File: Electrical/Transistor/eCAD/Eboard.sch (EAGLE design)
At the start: 22 parts

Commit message: put resistor in series and resolved trace issues on board
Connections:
- new net N$1: D1.C, R4.1
- net 5V: no longer R4.2
- net GND: now also R4.2; no longer D1.C, R4.1
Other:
- moved on the sheet: D1, R4
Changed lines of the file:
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@@
 <instance part="JP6" gate="A" x="116.84" y="170.18" rot="R180"/>
 <instance part="STEER_ENC" gate="A" x="203.2" y="76.2"/>
-<instance part="D1" gate="G$1" x="83.82" y="86.36" rot="R90"/>
+<instance part="D1" gate="G$1" x="86.36" y="96.52"/>
 <instance part="LIGHT_A_B" gate="G$1" x="193.04" y="121.92"/>
-<instance part="R4" gate="G$1" x="86.36" y="96.52" rot="R180"/>
+<instance part="R4" gate="G$1" x="86.36" y="86.36" rot="R270"/>
 <instance part="GND1" gate="1" x="134.62" y="55.88"/>
 <instance part="GND3" gate="1" x="147.32" y="116.84"/>
-<instance part="GND4" gate="1" x="99.06" y="88.9"/>
+<instance part="GND4" gate="1" x="86.36" y="78.74"/>
 <instance part="SUPPLY2" gate="G$1" x="165.1" y="83.82"/>
 <instance part="R5" gate="G$1" x="170.18" y="78.74" rot="R180"/>
@@
 <instance part="GND8" gate="1" x="134.62" y="121.92"/>
 <instance part="GND9" gate="1" x="66.04" y="106.68"/>
-<instance part="SUPPLY3" gate="G$1" x="71.12" y="91.44"/>
+<instance part="SUPPLY3" gate="G$1" x="86.36" y="99.06"/>
 <instance part="SUPPLY4" gate="G$1" x="58.42" y="139.7"/>
 </instances>
@@
 </segment>
 <segment>
-<pinref part="D1" gate="G$1" pin="A"/>
-<pinref part="R4" gate="G$1" pin="2"/>
-<wire x1="81.28" y1="86.36" x2="81.28" y2="91.44" width="0.1524" layer="91"/>
-<pinref part="SUPPLY3" gate="G$1" pin="5V"/>
-<wire x1="81.28" y1="91.44" x2="81.28" y2="96.52" width="0.1524" layer="91"/>
-<wire x1="71.12" y1="91.44" x2="81.28" y2="91.44" width="0.1524" layer="91"/>
-<junction x="81.28" y="91.44"/>
-</segment>
-<segment>
 <pinref part="R5" gate="G$1" pin="2"/>
 <pinref part="SUPPLY2" gate="G$1" pin="5V"/>
 <wire x1="165.1" y1="78.74" x2="165.1" y2="83.82" width="0.1524" layer="91"/>
+</segment>
+<segment>
+<pinref part="D1" gate="G$1" pin="A"/>
+<pinref part="SUPPLY3" gate="G$1" pin="5V"/>
 </segment>
 </net>
@@
 </segment>
 <segment>
-<pinref part="D1" gate="G$1" pin="C"/>
-<wire x1="88.9" y1="86.36" x2="91.44" y2="86.36" width="0.1524" layer="91"/>
-<wire x1="91.44" y1="86.36" x2="91.44" y2="91.44" width="0.1524" layer="91"/>
-<pinref part="R4" gate="G$1" pin="1"/>
-<wire x1="91.44" y1="91.44" x2="91.44" y2="96.52" width="0.1524" layer="91"/>
-<wire x1="91.44" y1="91.44" x2="99.06" y2="91.44" width="0.1524" layer="91"/>
-<junction x="91.44" y="91.44"/>
-<pinref part="GND4" gate="1" pin="GND"/>
-</segment>
-<segment>
 <pinref part="UART2" gate="A" pin="6"/>
 <wire x1="160.02" y1="172.72" x2="180.34" y2="172.72" width="0.1524" layer="91"/>
@@
 <pinref part="GND3" gate="1" pin="GND"/>
 <wire x1="152.4" y1="119.38" x2="147.32" y2="119.38" width="0.1524" layer="91"/>
+</segment>
+<segment>
+<pinref part="R4" gate="G$1" pin="2"/>
+<pinref part="GND4" gate="1" pin="GND"/>
 </segment>
 </net>
@@
 </segment>
 </net>
+<net name="N$1" class="0">
+<segment>
+<pinref part="R4" gate="G$1" pin="1"/>
+<pinref part="D1" gate="G$1" pin="C"/>
+</segment>
+</net>

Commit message: changed indicator to have pull up resistor in series that has resistance of 60, changed traces to be right size, added 5V silkscreen for indicator led
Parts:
- R4: value 1k -> 60
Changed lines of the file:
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@@
 <part name="D1" library="SparkFun-LED" library_urn="urn:adsk.eagle:library:529" deviceset="LED" device="1206" package3d_urn="urn:adsk.eagle:package:39352/1"/>
 <part name="LIGHT_A_B" library="SparkFun-Connectors" library_urn="urn:adsk.eagle:library:513" deviceset="CONN_04" device="" package3d_urn="urn:adsk.eagle:package:38085/1"/>
-<part name="R4" library="SparkFun-Resistors" library_urn="urn:adsk.eagle:library:532" deviceset="1KOHM" device="-HORIZ-1/4W-5%" package3d_urn="urn:adsk.eagle:package:39658/1" value="1k"/>
+<part name="R4" library="SparkFun-Resistors" library_urn="urn:adsk.eagle:library:532" deviceset="1KOHM" device="-HORIZ-1/4W-5%" package3d_urn="urn:adsk.eagle:package:39658/1" value="60"/>
 <part name="GND1" library="SparkFun-PowerSymbols" library_urn="urn:adsk.eagle:library:530" deviceset="GND" device=""/>
 <part name="GND3" library="SparkFun-PowerSymbols" library_urn="urn:adsk.eagle:library:530" deviceset="GND" device=""/>

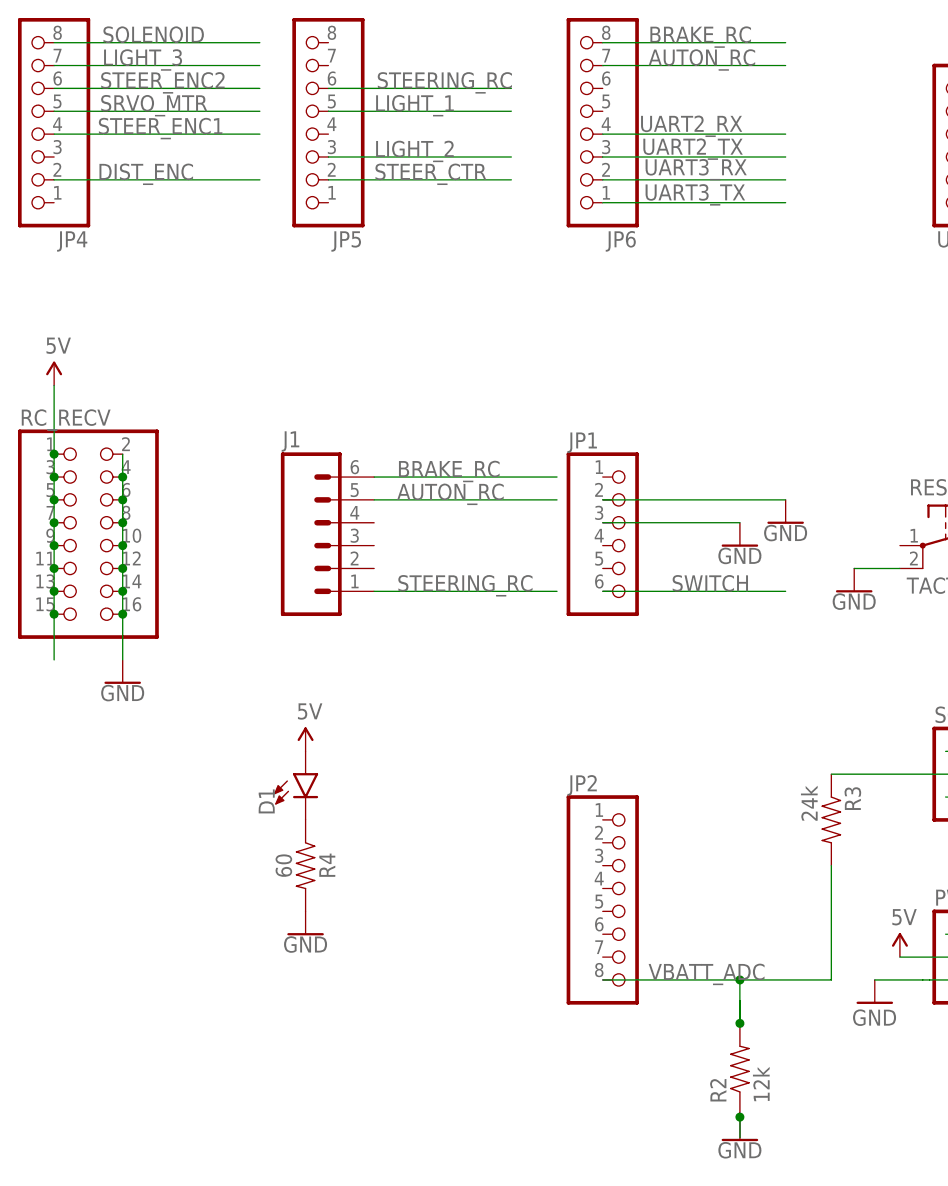
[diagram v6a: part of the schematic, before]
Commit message: updated dimensions, reversed the JP1 pin set, reversed JP2 so that VBATT would be in pin A0, reversed all thre three-pin connections to match existing pin plug in configuration, updated R4 resistor to be 120 ohms, switched encA and encB positions
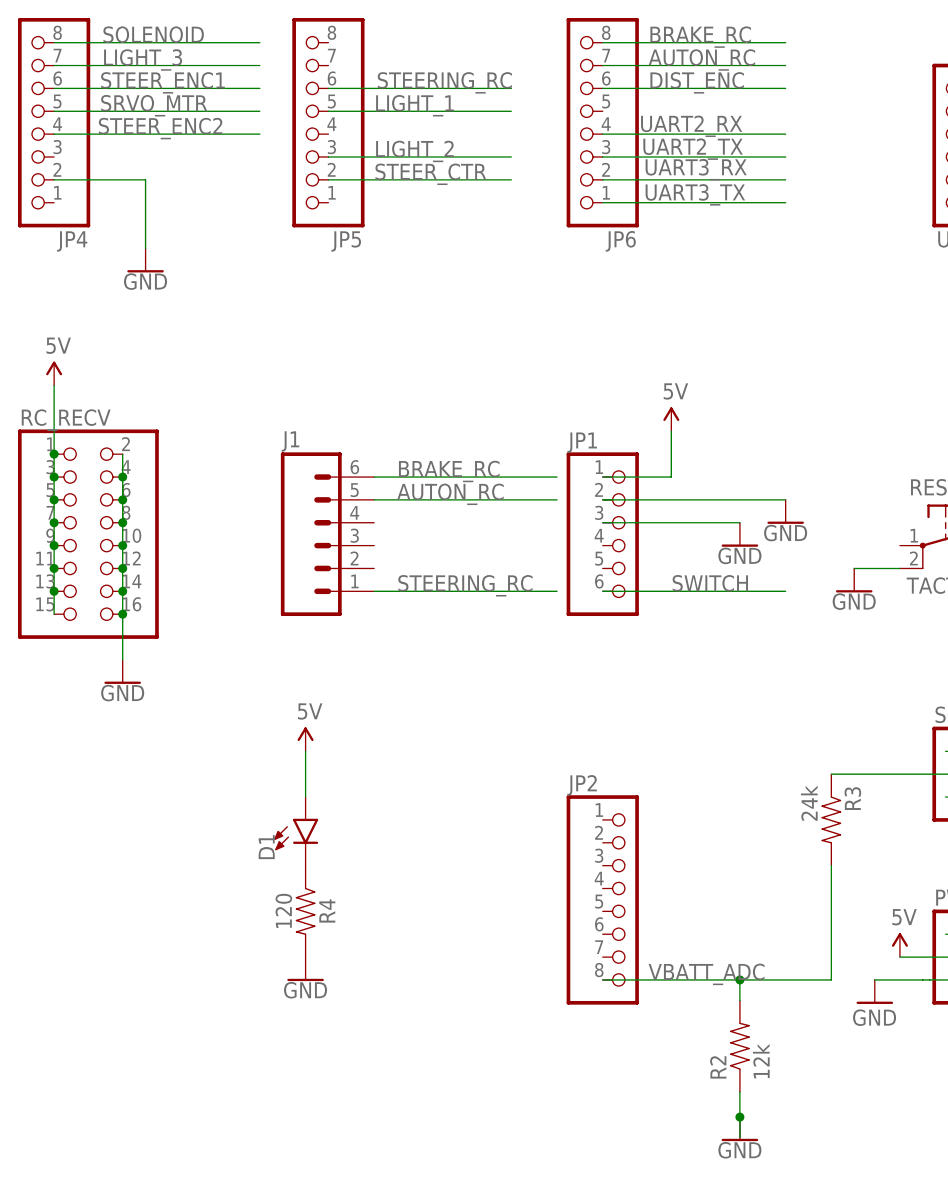
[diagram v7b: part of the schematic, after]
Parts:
- R4: value 60 -> 120
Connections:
- net 5V: now also JP1.1
- net DIST_ENC: now also JP6.6; no longer JP4.2
- net GND: now also JP4.2
- net STEER_ENC1: now also JP4.6; no longer JP4.4
- net STEER_ENC2: now also JP4.4; no longer JP4.6
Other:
- moved on the sheet: D1, R2, R4
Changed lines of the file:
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@@
 <part name="D1" library="SparkFun-LED" library_urn="urn:adsk.eagle:library:529" deviceset="LED" device="1206" package3d_urn="urn:adsk.eagle:package:39352/1"/>
 <part name="LIGHT_A_B" library="SparkFun-Connectors" library_urn="urn:adsk.eagle:library:513" deviceset="CONN_04" device="" package3d_urn="urn:adsk.eagle:package:38085/1"/>
-<part name="R4" library="SparkFun-Resistors" library_urn="urn:adsk.eagle:library:532" deviceset="1KOHM" device="-HORIZ-1/4W-5%" package3d_urn="urn:adsk.eagle:package:39658/1" value="60"/>
+<part name="R4" library="SparkFun-Resistors" library_urn="urn:adsk.eagle:library:532" deviceset="1KOHM" device="-HORIZ-1/4W-5%" package3d_urn="urn:adsk.eagle:package:39658/1" value="120"/>
 <part name="GND1" library="SparkFun-PowerSymbols" library_urn="urn:adsk.eagle:library:530" deviceset="GND" device=""/>
 <part name="GND3" library="SparkFun-PowerSymbols" library_urn="urn:adsk.eagle:library:530" deviceset="GND" device=""/>
@@
 <part name="SUPPLY3" library="SparkFun-Aesthetics" deviceset="5V" device=""/>
 <part name="SUPPLY4" library="SparkFun-Aesthetics" deviceset="5V" device=""/>
+<part name="SUPPLY5" library="SparkFun-Aesthetics" deviceset="5V" device=""/>
+<part name="GND10" library="SparkFun-PowerSymbols" library_urn="urn:adsk.eagle:library:530" deviceset="GND" device=""/>
 </parts>
 <sheets>
@@
 <instance part="SUPPLY1" gate="G$1" x="152.4" y="76.2"/>
 <instance part="RESET" gate="G$1" x="157.48" y="121.92"/>
-<instance part="R2" gate="G$1" x="134.62" y="63.754" rot="R90"/>
+<instance part="R2" gate="G$1" x="134.62" y="66.294" rot="R90"/>
 <instance part="R3" gate="G$1" x="144.78" y="91.44" rot="R270"/>
 <instance part="P+2" gate="1" x="213.36" y="99.06"/>
@@
 <instance part="JP6" gate="A" x="116.84" y="170.18" rot="R180"/>
 <instance part="STEER_ENC" gate="A" x="203.2" y="76.2"/>
-<instance part="D1" gate="G$1" x="86.36" y="96.52"/>
+<instance part="D1" gate="G$1" x="86.36" y="91.44"/>
 <instance part="LIGHT_A_B" gate="G$1" x="193.04" y="121.92"/>
-<instance part="R4" gate="G$1" x="86.36" y="86.36" rot="R270"/>
+<instance part="R4" gate="G$1" x="86.36" y="81.28" rot="R270"/>
 <instance part="GND1" gate="1" x="134.62" y="55.88"/>
 <instance part="GND3" gate="1" x="147.32" y="116.84"/>
-<instance part="GND4" gate="1" x="86.36" y="78.74"/>
+<instance part="GND4" gate="1" x="86.36" y="73.66"/>
 <instance part="SUPPLY2" gate="G$1" x="165.1" y="83.82"/>
 <instance part="R5" gate="G$1" x="170.18" y="78.74" rot="R180"/>
@@
 <instance part="SUPPLY3" gate="G$1" x="86.36" y="99.06"/>
 <instance part="SUPPLY4" gate="G$1" x="58.42" y="139.7"/>
+<instance part="SUPPLY5" gate="G$1" x="127" y="134.62"/>
+<instance part="GND10" gate="1" x="68.58" y="152.4"/>
 </instances>
 <busses>
@@
 <pinref part="RC_RECV" gate="A" pin="15"/>
 <wire x1="58.42" y1="114.3" x2="58.42" y2="116.84" width="0.1524" layer="91"/>
-<wire x1="58.42" y1="114.3" x2="58.42" y2="109.22" width="0.1524" layer="91"/>
-<junction x="58.42" y="114.3"/>
 <pinref part="SUPPLY4" gate="G$1" pin="5V"/>
 <wire x1="58.42" y1="132.08" x2="58.42" y2="139.7" width="0.1524" layer="91"/>
@@
 <pinref part="D1" gate="G$1" pin="A"/>
 <pinref part="SUPPLY3" gate="G$1" pin="5V"/>
+<wire x1="86.36" y1="93.98" x2="86.36" y2="99.06" width="0.1524" layer="91"/>
+</segment>
+<segment>
+<pinref part="JP1" gate="A" pin="1"/>
+<wire x1="119.38" y1="129.54" x2="127" y2="129.54" width="0.1524" layer="91"/>
+<wire x1="127" y1="129.54" x2="127" y2="134.62" width="0.1524" layer="91"/>
+<pinref part="SUPPLY5" gate="G$1" pin="5V"/>
 </segment>
 </net>
@@
 <segment>
 <pinref part="R2" gate="G$1" pin="1"/>
-<wire x1="134.62" y1="58.674" x2="134.62" y2="58.42" width="0.1524" layer="91"/>
+<wire x1="134.62" y1="61.214" x2="134.62" y2="58.42" width="0.1524" layer="91"/>
 <pinref part="GND1" gate="1" pin="GND"/>
 <wire x1="134.62" y1="58.42" x2="134.62" y2="56.134" width="0.1524" layer="91"/>
@@
 <pinref part="GND3" gate="1" pin="GND"/>
 <wire x1="152.4" y1="119.38" x2="147.32" y2="119.38" width="0.1524" layer="91"/>
+</segment>
+<segment>
+<pinref part="JP4" gate="A" pin="2"/>
+<wire x1="58.42" y1="162.56" x2="68.58" y2="162.56" width="0.1524" layer="91"/>
+<wire x1="68.58" y1="162.56" x2="68.58" y2="154.94" width="0.1524" layer="91"/>
+<pinref part="GND10" gate="1" pin="GND"/>
 </segment>
 <segment>
@@
 </segment>
 <segment>
-<pinref part="JP4" gate="A" pin="2"/>
-<label x="63.246" y="162.56" size="1.778" layer="95"/>
-<wire x1="58.42" y1="162.56" x2="81.28" y2="162.56" width="0.1524" layer="91"/>
+<pinref part="JP6" gate="A" pin="6"/>
+<wire x1="119.38" y1="172.72" x2="139.7" y2="172.72" width="0.1524" layer="91"/>
+<label x="124.46" y="172.72" size="1.778" layer="95"/>
 </segment>
 </net>
@@
 </segment>
 <segment>
+<pinref part="JP4" gate="A" pin="6"/>
+<label x="63.5" y="172.72" size="1.778" layer="95"/>
+<wire x1="58.42" y1="172.72" x2="81.28" y2="172.72" width="0.1524" layer="91"/>
+</segment>
+</net>
+<net name="STEER_ENC2" class="0">
+<segment>
+<pinref part="STEER_ENC" gate="A" pin="2"/>
+<label x="205.74" y="78.74" size="1.778" layer="95"/>
+<wire x1="200.66" y1="78.74" x2="223.52" y2="78.74" width="0.1524" layer="91"/>
+</segment>
+<segment>
 <pinref part="JP4" gate="A" pin="4"/>
 <label x="63.246" y="167.64" size="1.778" layer="95"/>
@@
 </segment>
 </net>
-<net name="STEER_ENC2" class="0">
-<segment>
-<pinref part="STEER_ENC" gate="A" pin="2"/>
-<label x="205.74" y="78.74" size="1.778" layer="95"/>
-<wire x1="200.66" y1="78.74" x2="223.52" y2="78.74" width="0.1524" layer="91"/>
-</segment>
-<segment>
-<pinref part="JP4" gate="A" pin="6"/>
-<label x="63.5" y="172.72" size="1.778" layer="95"/>
-<wire x1="58.42" y1="172.72" x2="81.28" y2="172.72" width="0.1524" layer="91"/>
-</segment>
-</net>
 <net name="UART2_TX" class="0">
 <segment>
@@
 <segment>
 <pinref part="R2" gate="G$1" pin="2"/>
-<wire x1="134.62" y1="68.834" x2="134.62" y2="71.374" width="0.1524" layer="91"/>
 <pinref part="JP2" gate="A" pin="8"/>
 <label x="124.46" y="73.66" size="1.778" layer="95"/>
@@
 <wire x1="134.62" y1="73.66" x2="144.78" y2="73.66" width="0.1524" layer="91"/>
 <wire x1="144.78" y1="73.66" x2="144.78" y2="86.36" width="0.1524" layer="91"/>
-<wire x1="134.62" y1="68.834" x2="134.62" y2="73.66" width="0.1524" layer="91"/>
-<junction x="134.62" y="68.834"/>
+<wire x1="134.62" y1="71.374" x2="134.62" y2="73.66" width="0.1524" layer="91"/>
 <junction x="134.62" y="73.66"/>
 </segment>
@@
 <net name="N$1" class="0">
 <segment>
+<pinref part="D1" gate="G$1" pin="C"/>
 <pinref part="R4" gate="G$1" pin="1"/>
-<pinref part="D1" gate="G$1" pin="C"/>
-</segment>
-</net>
+</segment>
+</net>
